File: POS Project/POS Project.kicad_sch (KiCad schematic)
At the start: 60 parts, among them J1 JST_2mm_LiPo, J2 Conn_01x05_Socket, P1 USB_C_Plug_USB2.0, SW1 SW_Push, SW2 SW_Push, U1 MCP73831-2-OT, U2 SMN-303, U4 SMF05C, U8 ESP32-S3-WROOM-1-N8R8, U9 SGM2212-3.3

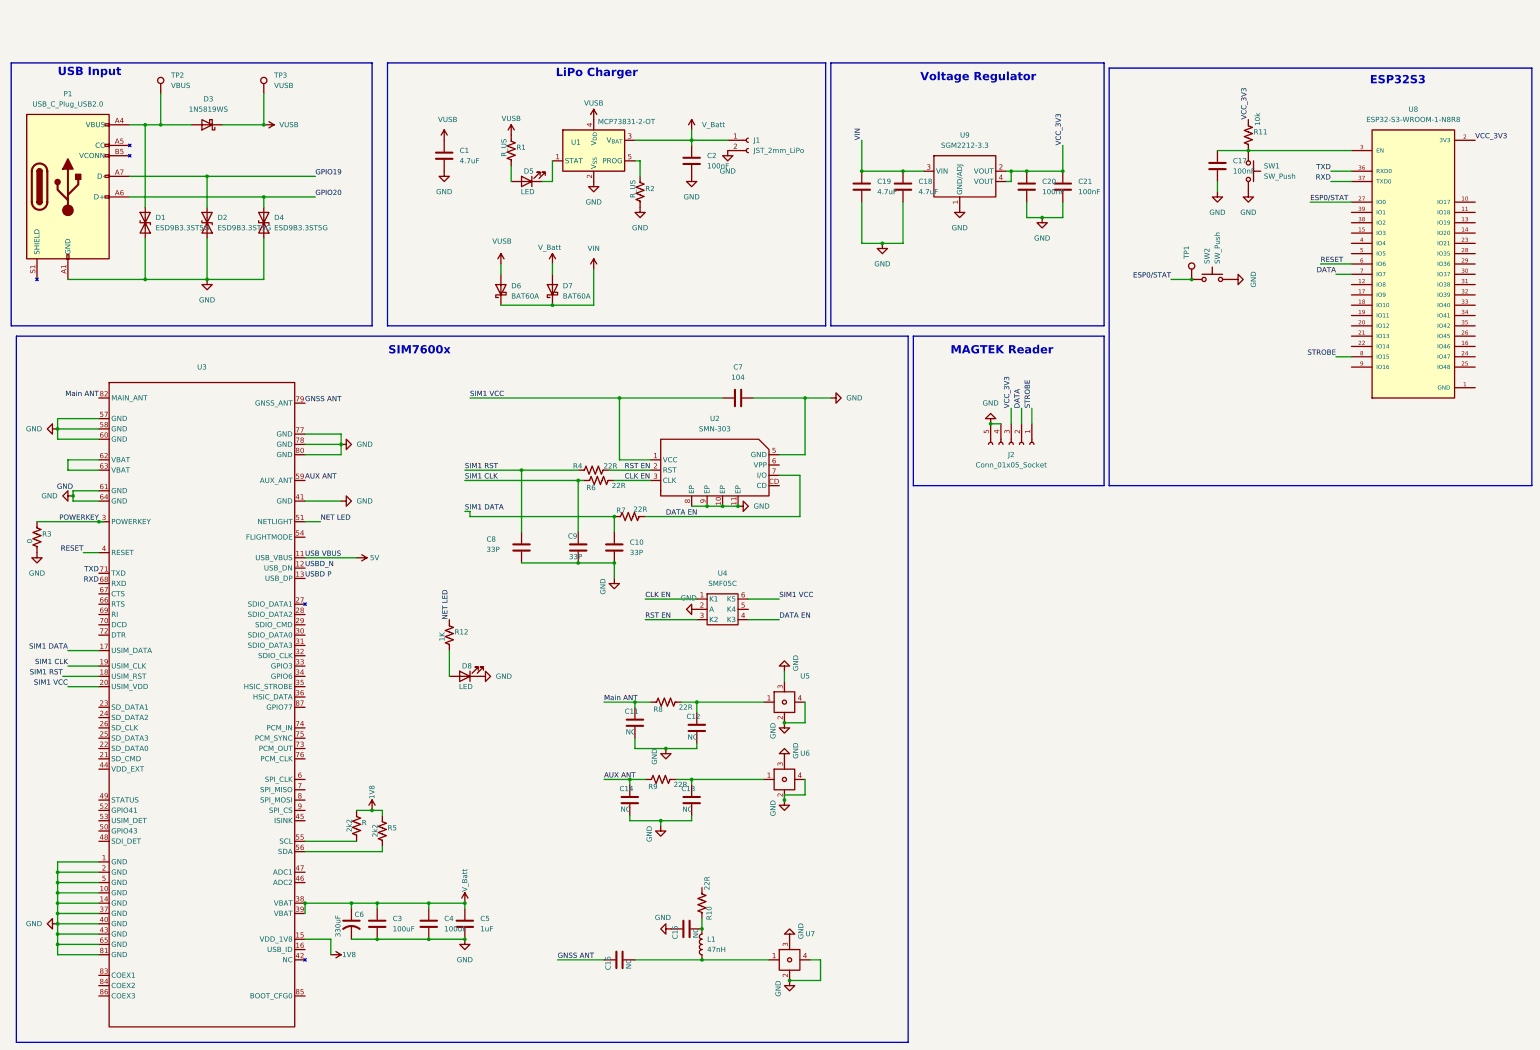
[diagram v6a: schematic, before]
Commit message: added PCB board
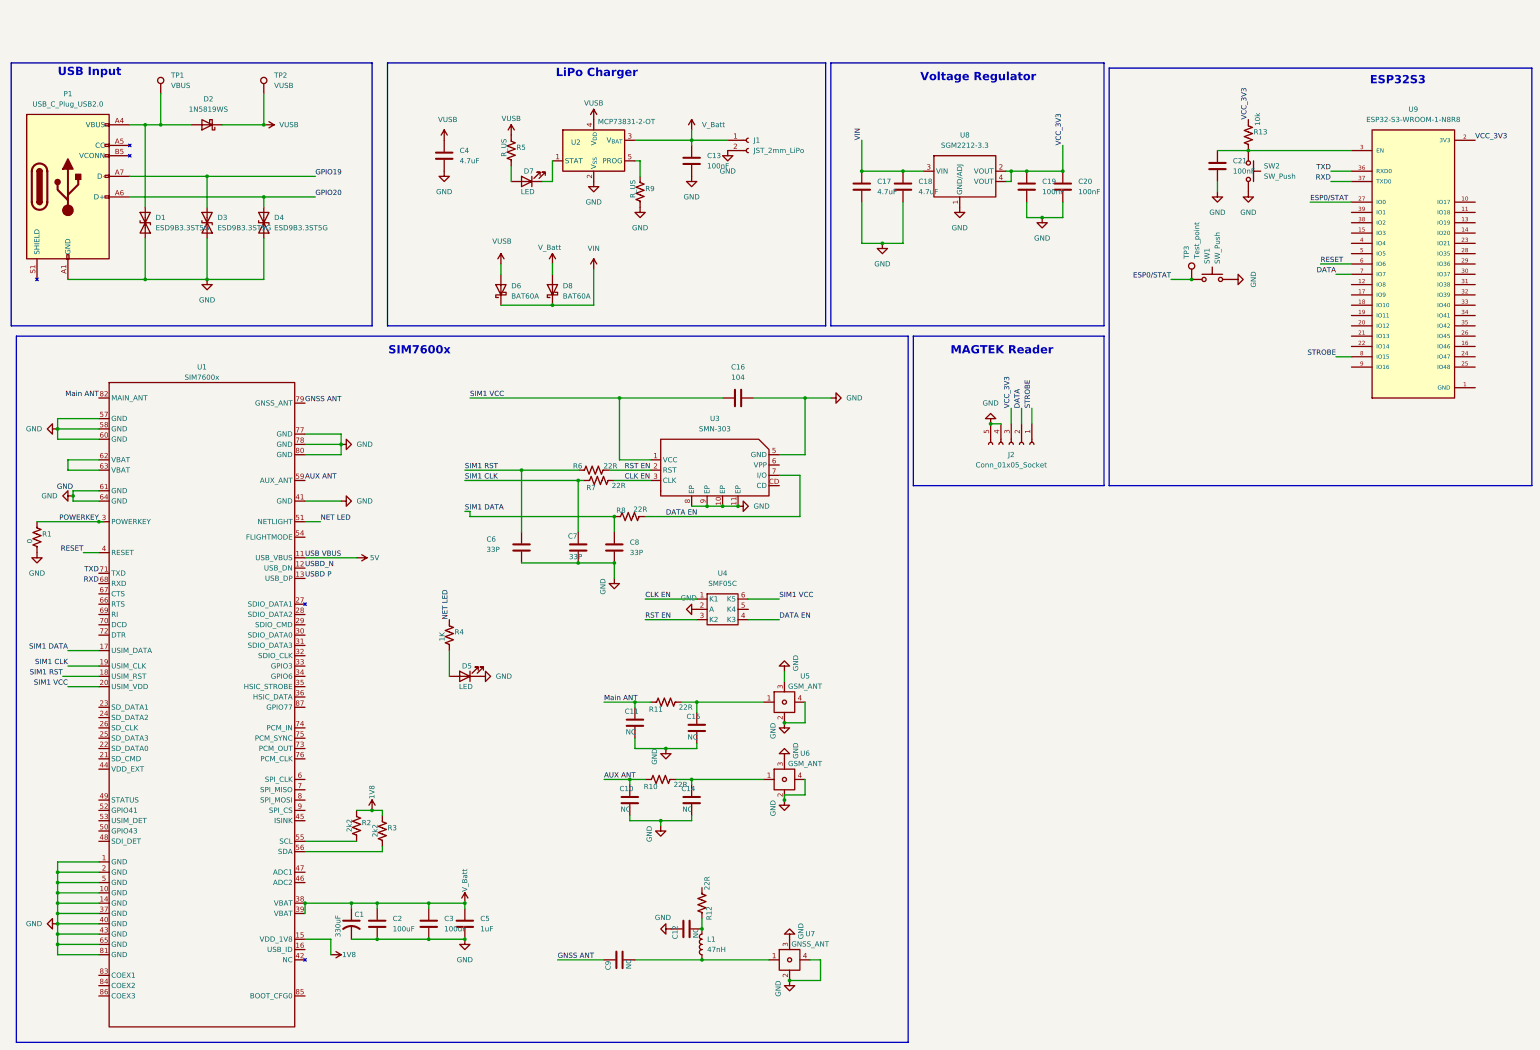
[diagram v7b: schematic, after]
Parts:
- C17: renamed from C19; footprint (none) -> Capacitor_SMD:C_0805_2012Metric
- C18: footprint (none) -> Capacitor_SMD:C_0805_2012Metric
- C4: renamed from C1; footprint (none) -> Capacitor_SMD:C_0805_2012Metric
- R1: renamed from R3; footprint (none) -> Resistor_SMD:R_0805_2012Metric
- R10: renamed from R9; footprint (none) -> Resistor_SMD:R_0805_2012Metric
- R11: renamed from R8; footprint (none) -> Resistor_SMD:R_0805_2012Metric
- R12: renamed from R10; footprint (none) -> Resistor_SMD:R_0805_2012Metric
- R13: renamed from R11; footprint (none) -> Resistor_SMD:R_0805_2012Metric
- R2: renamed from R; footprint (none) -> Resistor_SMD:R_0805_2012Metric
- R3: renamed from R5; footprint (none) -> Resistor_SMD:R_0805_2012Metric
- R4: renamed from R12; footprint (none) -> Resistor_SMD:R_0805_2012Metric
- R5: renamed from R1; footprint Connector_USB:USB_C_Receptacle_GCT_USB4105-xx-A_16P_TopMnt_Horizontal -> Resistor_SMD:R_0805_2012Metric
- R6: renamed from R4; footprint (none) -> Resistor_SMD:R_0805_2012Metric
- R7: renamed from R6; footprint (none) -> Resistor_SMD:R_0805_2012Metric
- R8: renamed from R7; footprint (none) -> Resistor_SMD:R_0805_2012Metric
- R9: renamed from R2; footprint Connector_USB:USB_C_Receptacle_GCT_USB4105-xx-A_16P_TopMnt_Horizontal -> Resistor_SMD:R_0805_2012Metric
- SW1: renamed from SW2; footprint (none) -> Button_Switch_THT:SW_PUSH_6mm
- SW2: renamed from SW1; footprint (none) -> Button_Switch_THT:SW_PUSH_6mm
- TP1: renamed from TP2; footprint (none) -> TestPoint:TestPoint_Keystone_5019_Miniature
- TP2: renamed from TP3; footprint (none) -> TestPoint:TestPoint_Keystone_5019_Miniature
- TP3: renamed from TP1; value ~ -> Test_point; footprint (none) -> TestPoint:TestPoint_Keystone_5019_Miniature
- U1: renamed from U3; value ~ -> SIM7600x; footprint (none) -> SIM7600G:IC_SIM7600G
- U4: footprint (none) -> Package_TO_SOT_SMD:SOT-363_SC-70-6
- U5, U6: value ~ -> GSM_ANT; footprint (none) -> Connector_Coaxial:U.FL_Molex_MCRF_73412-0110_Vertical
- U7: value ~ -> GNSS_ANT; footprint (none) -> Connector_Coaxial:U.FL_Molex_MCRF_73412-0110_Vertical
- renumbered C6 to C1, C14 to C10, C15 to C12, C2 to C13, C13 to C14, C12 to C15, C7 to C16, C20 to C19, C3 to C2, C21 to C20, C17 to C21, C4 to C3, C8 to C6, C9 to C7, C10 to C8, C16 to C9, D3 to D2, D2 to D3, D8 to D5, D5 to D7, D7 to D8, U1 to U2, U2 to U3, U9 to U8, U8 to U9

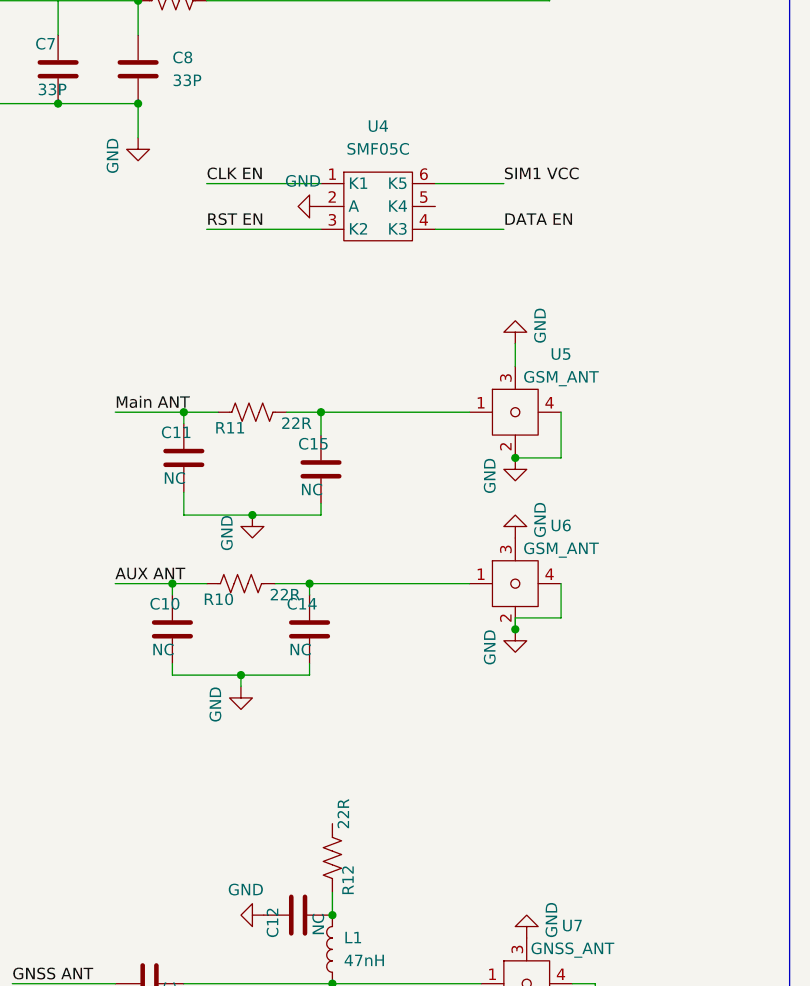
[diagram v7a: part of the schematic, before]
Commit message: organized PCB components
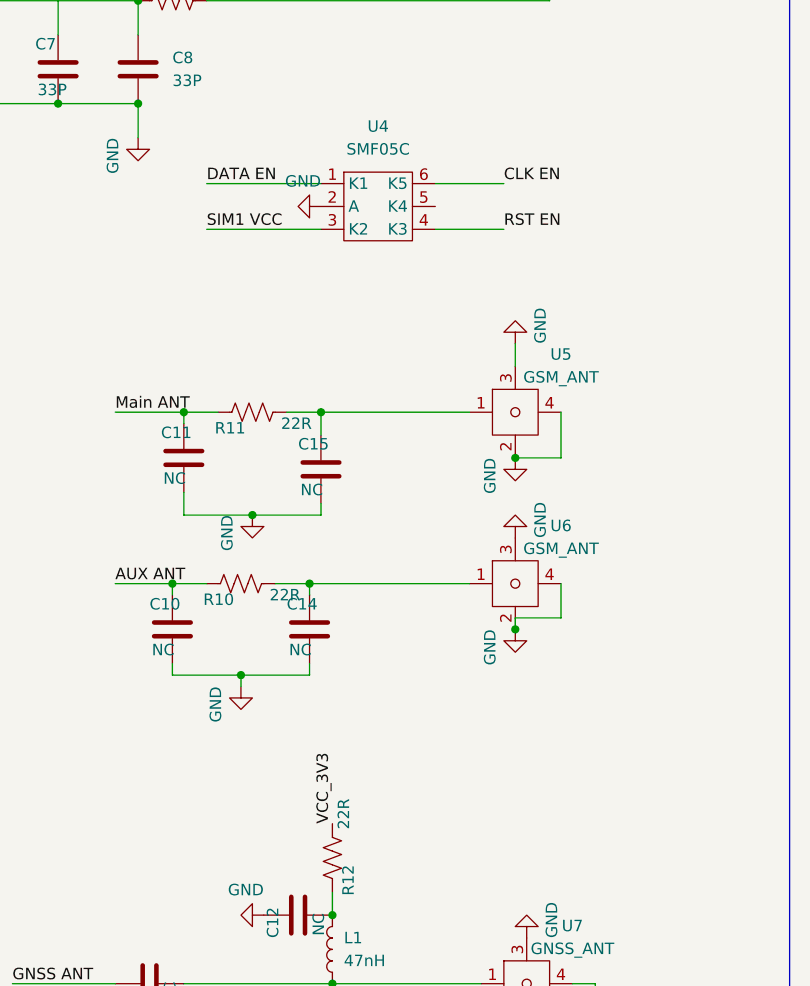
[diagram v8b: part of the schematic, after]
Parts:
- TP1, TP2, TP3: footprint TestPoint:TestPoint_Keystone_5019_Miniature -> TestPoint:TestPoint_Pad_1.0x1.0mm
- U3: footprint (none) -> SMN-303:SIM-SMD_SMN-303
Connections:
- net CLK EN: now also U4.6 (K5); no longer U4.1 (K1)
- net DATA EN: now also U4.1 (K1); no longer U4.4 (K3)
- net RST EN: now also U4.4 (K3); no longer U4.3 (K2)
- net SIM1 VCC: now also U4.3 (K2); no longer U4.6 (K5)
- net VCC_3V3: now also R12.2
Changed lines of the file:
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@@
 		)
 	)
-	(label "SIM1 VCC"
+	(label "CLK EN"
 		(at 200.66 144.78 0)
 		(effects
@@
 		)
 	)
-	(label "DATA EN"
+	(label "RST EN"
 		(at 200.66 149.86 0)
 		(effects
@@
 		)
 	)
-	(label "CLK EN"
+	(label "DATA EN"
 		(at 167.64 144.78 0)
 		(effects
@@
 		)
 	)
+	(label "VCC_3V3"
+		(at 181.61 215.9 90)
+		(effects
+			(font
+				(size 1.27 1.27)
+			)
+			(justify left bottom)
+		)
+	)
 	(label "USB VBUS"
 		(at 83.82 134.62 0)
@@
 		)
 	)
-	(label "RST EN"
+	(label "SIM1 VCC"
 		(at 167.64 149.86 0)
 		(effects
@@
 			)
 		)
-		(property "Footprint" "TestPoint:TestPoint_Keystone_5019_Miniature"
+		(property "Footprint" "TestPoint:TestPoint_Pad_1.0x1.0mm"
 			(at 307.34 66.04 0)
 			(effects
@@
 			)
 		)
-		(property "Footprint" ""
+		(property "Footprint" "SMN-303:SIM-SMD_SMN-303"
 			(at 184.15 113.03 0)
 			(effects
@@
 			)
 		)
-		(property "Footprint" "TestPoint:TestPoint_Keystone_5019_Miniature"
+		(property "Footprint" "TestPoint:TestPoint_Pad_1.0x1.0mm"
 			(at 53.34 20.32 0)
 			(effects
@@
 			)
 		)
-		(property "Footprint" "TestPoint:TestPoint_Keystone_5019_Miniature"
+		(property "Footprint" "TestPoint:TestPoint_Pad_1.0x1.0mm"
 			(at 78.74 20.32 0)
 			(effects
